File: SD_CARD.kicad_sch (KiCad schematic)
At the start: 6 parts, among them IC1 ECP5-BGA256, J4 Micro_SD_Card, U7 OSC_25M

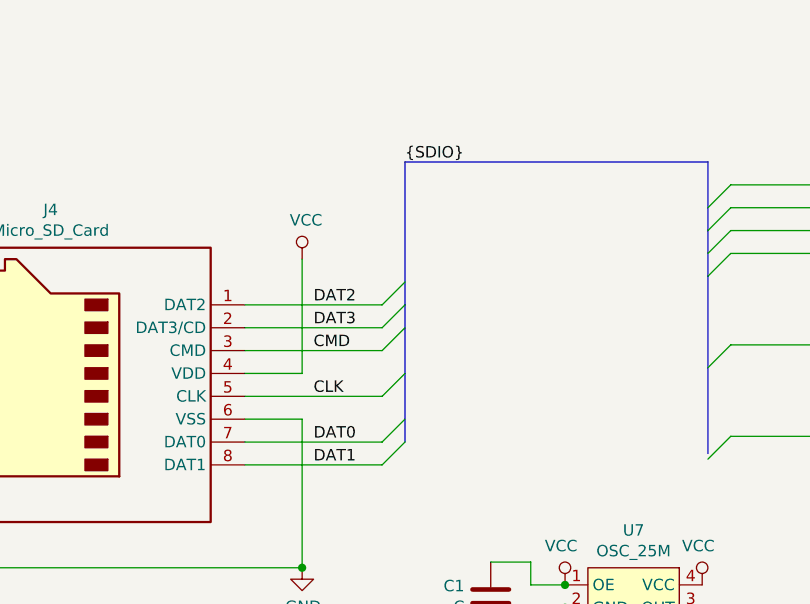
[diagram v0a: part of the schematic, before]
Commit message: Add semi-critical resistor values
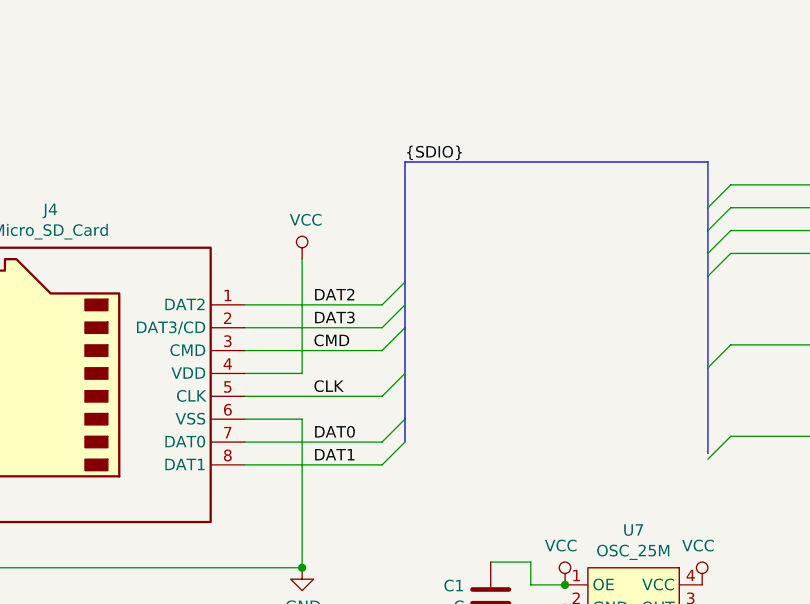
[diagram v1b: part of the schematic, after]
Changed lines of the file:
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@@
-(kicad_sch (version 20200618) (host eeschema "5.99.0-unknown-7340c97~102~ubuntu20.04.1")
-  (page 6 6)
+(kicad_sch (version 20200618) (host eeschema "5.99.0-unknown-e9da02e~102~ubuntu20.04.1")
+  (page 1 6)
   (paper "A4")
   (bus_alias "SDIO" (members "DAT[0..3]" "CMD" "CLK"))
@@
     (stroke (width 0) (type solid) (color 0 0 0 0))
   )
-  (bus (pts (xy 149.86 64.135) (xy 149.86 80.01))
+  (bus (pts (xy 149.86 64.135) (xy 149.86 77.47))
     (stroke (width 0) (type solid) (color 0 0 0 0))
   )
-  (bus (pts (xy 149.86 80.01) (xy 149.86 87.63))
+  (bus (pts (xy 149.86 77.47) (xy 149.86 82.55))
     (stroke (width 0) (type solid) (color 0 0 0 0))
   )
-  (bus (pts (xy 149.86 87.63) (xy 149.86 95.25))
+  (bus (pts (xy 149.86 82.55) (xy 149.86 92.71))
     (stroke (width 0) (type solid) (color 0 0 0 0))
   )
+  (bus (pts (xy 149.86 92.71) (xy 149.86 95.25))
+    (stroke (width 0) (type solid) (color 0 0 0 0))
+  )

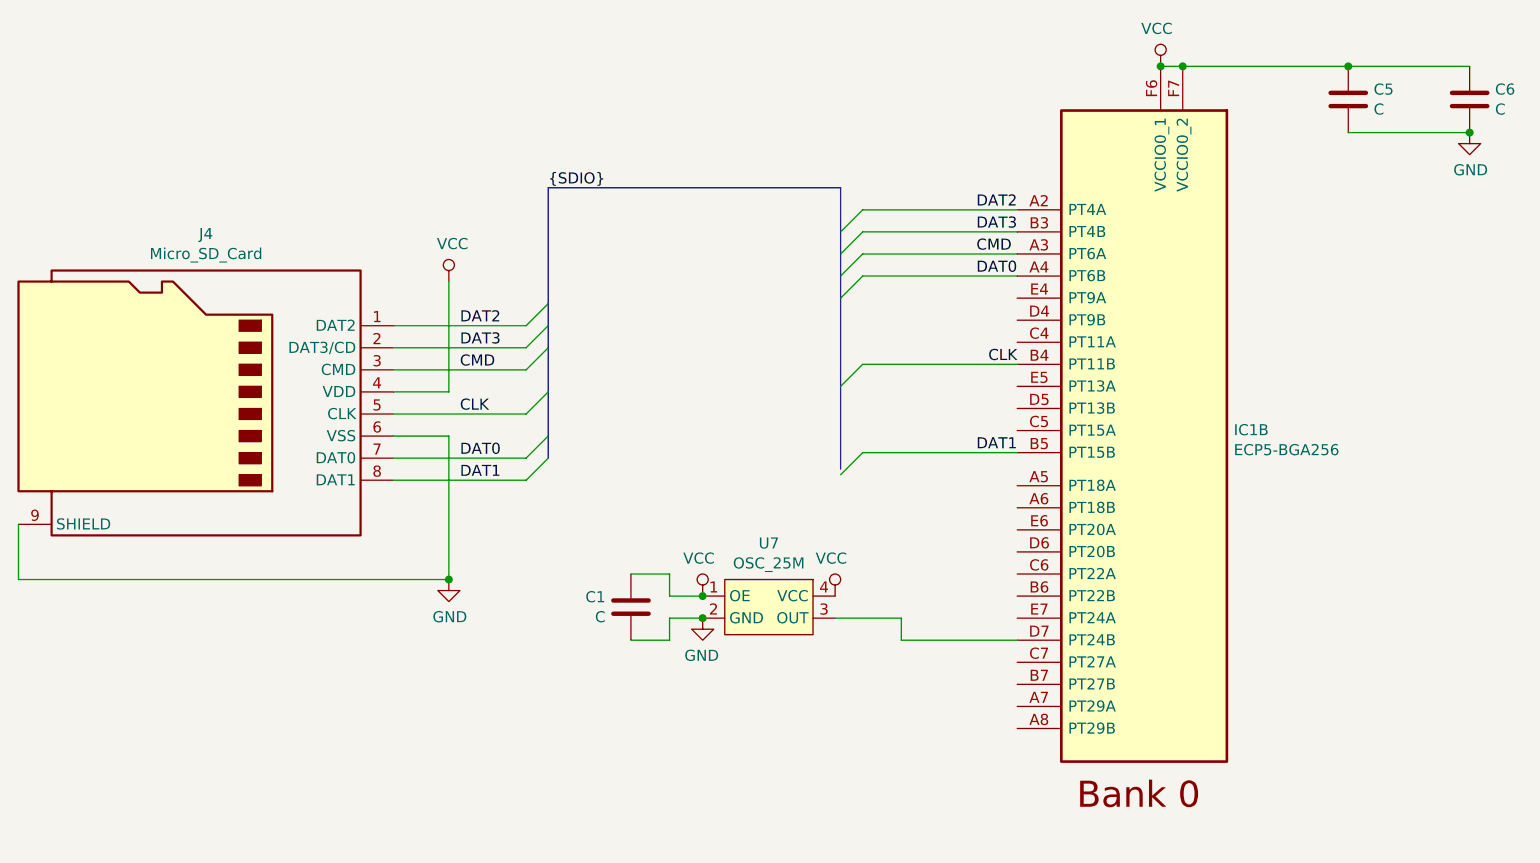
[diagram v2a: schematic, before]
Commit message: Change oscillator to SI5315, change RGB LED
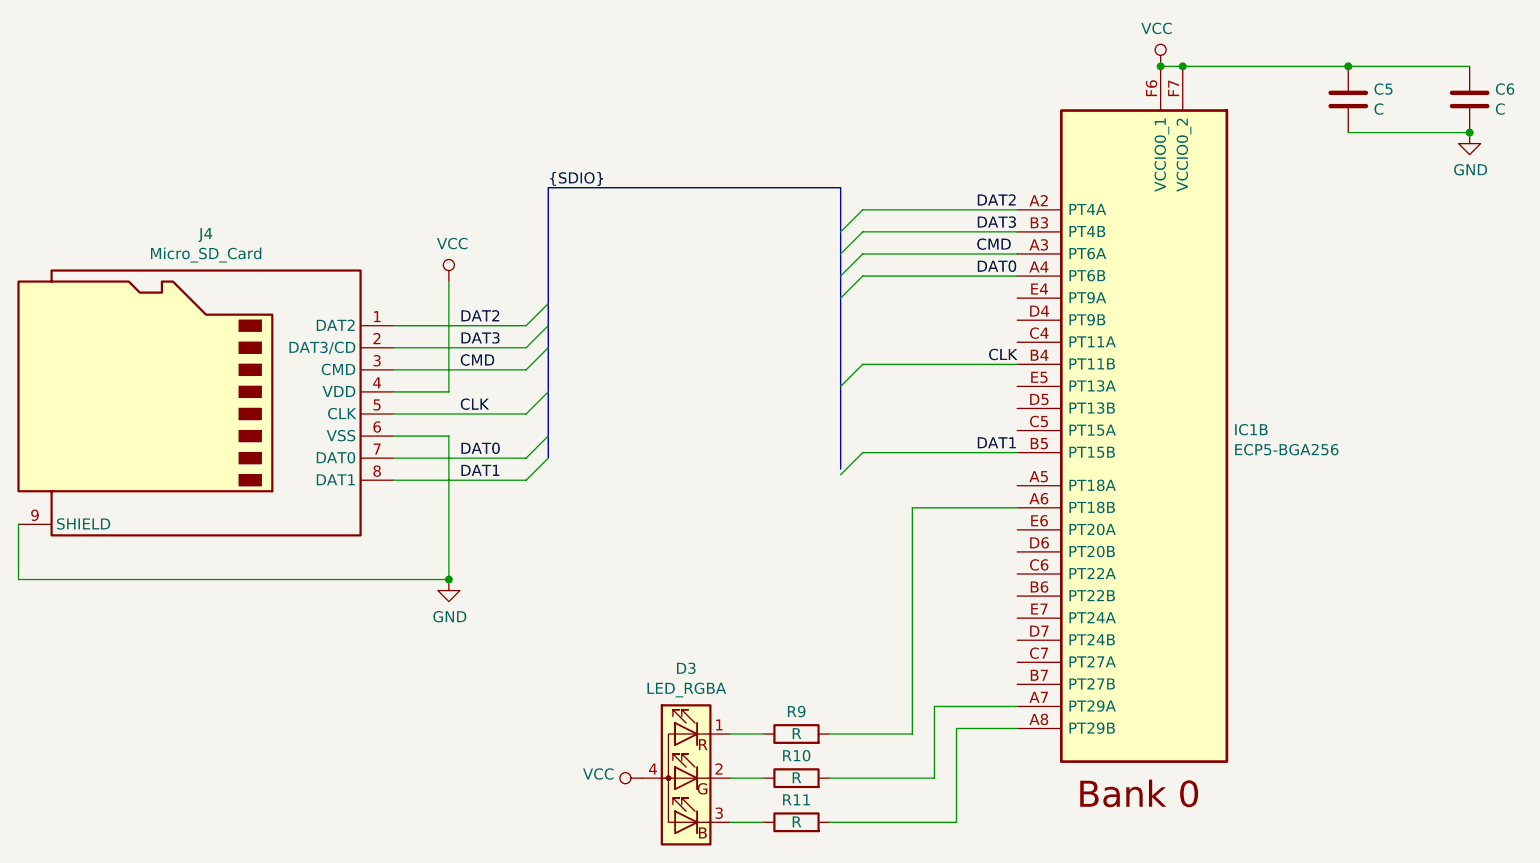
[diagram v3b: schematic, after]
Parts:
- removed C1: C, Capacitor_SMD:C_0402_1005Metric, symbol Device:C
- removed U7: OSC_25M, mini-mipi:SOIC-4, symbol mini_mipi:OSC_25M
- added D3: LED_RGBA, mini-mipi:LED_0404, symbol Device:LED_RGBA
- added R10, R11, R9: R, Resistor_SMD:R_0402_1005Metric, symbol Device:R
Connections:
- net VCC: now also D3.4 (A)
- net at IC1.A6 (PT18B): now also R9.2
- net at IC1.A7 (PT29A): now also R10.2
- net at IC1.A8 (PT29B): now also R11.2
- new net: D3.1 (RK), R9.1
- new net: D3.2 (GK), R10.1
- new net: D3.3 (BK), R11.1
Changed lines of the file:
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@@
-(kicad_sch (version 20200714) (host eeschema "5.99.0-unknown-9f20c61~102~ubuntu20.04.1")
-  (page 1 6)
+(kicad_sch (version 20200714) (host eeschema "5.99.0-unknown-20c1492~102~ubuntu20.04.1")
+  (page 6 6)
   (paper "A4")
   (bus_alias "SDIO" (members "DAT[0..3]" "CMD" "CLK"))
   (junction (at 138.43 109.22) (diameter 0) (color 0 0 0 0))
-  (junction (at 167.64 111.125) (diameter 0) (color 0 0 0 0))
-  (junction (at 167.64 113.665) (diameter 0) (color 0 0 0 0))
   (junction (at 220.345 50.165) (diameter 0) (color 0 0 0 0))
   (junction (at 222.885 50.165) (diameter 0) (color 0 0 0 0))
@@
     (stroke (width 0) (type solid) (color 0 0 0 0))
   )
-  (wire (pts (xy 159.385 116.205) (xy 163.83 116.205))
-    (stroke (width 0) (type solid) (color 0 0 0 0))
-  )
-  (wire (pts (xy 163.83 108.585) (xy 159.385 108.585))
-    (stroke (width 0) (type solid) (color 0 0 0 0))
-  )
-  (wire (pts (xy 163.83 111.125) (xy 163.83 108.585))
-    (stroke (width 0) (type solid) (color 0 0 0 0))
-  )
-  (wire (pts (xy 163.83 113.665) (xy 167.64 113.665))
-    (stroke (width 0) (type solid) (color 0 0 0 0))
-  )
-  (wire (pts (xy 163.83 116.205) (xy 163.83 113.665))
-    (stroke (width 0) (type solid) (color 0 0 0 0))
-  )
-  (wire (pts (xy 167.64 111.125) (xy 163.83 111.125))
+  (wire (pts (xy 170.815 127) (xy 174.625 127))
+    (stroke (width 0) (type solid) (color 0 0 0 0))
+  )
+  (wire (pts (xy 170.815 132.08) (xy 174.625 132.08))
+    (stroke (width 0) (type solid) (color 0 0 0 0))
+  )
+  (wire (pts (xy 170.815 137.16) (xy 174.625 137.16))
+    (stroke (width 0) (type solid) (color 0 0 0 0))
+  )
+  (wire (pts (xy 182.245 132.08) (xy 194.31 132.08))
     (stroke (width 0) (type solid) (color 0 0 0 0))
   )
@@
     (stroke (width 0) (type solid) (color 0 0 0 0))
   )
-  (wire (pts (xy 190.5 113.665) (xy 182.88 113.665))
-    (stroke (width 0) (type solid) (color 0 0 0 0))
-  )
-  (wire (pts (xy 190.5 116.205) (xy 190.5 113.665))
-    (stroke (width 0) (type solid) (color 0 0 0 0))
-  )
-  (wire (pts (xy 203.835 116.205) (xy 190.5 116.205))
+  (wire (pts (xy 191.77 100.965) (xy 191.77 127))
+    (stroke (width 0) (type solid) (color 0 0 0 0))
+  )
+  (wire (pts (xy 191.77 100.965) (xy 203.835 100.965))
+    (stroke (width 0) (type solid) (color 0 0 0 0))
+  )
+  (wire (pts (xy 191.77 127) (xy 182.245 127))
+    (stroke (width 0) (type solid) (color 0 0 0 0))
+  )
+  (wire (pts (xy 194.31 123.825) (xy 203.835 123.825))
+    (stroke (width 0) (type solid) (color 0 0 0 0))
+  )
+  (wire (pts (xy 194.31 132.08) (xy 194.31 123.825))
+    (stroke (width 0) (type solid) (color 0 0 0 0))
+  )
+  (wire (pts (xy 196.85 126.365) (xy 196.85 137.16))
+    (stroke (width 0) (type solid) (color 0 0 0 0))
+  )
+  (wire (pts (xy 196.85 137.16) (xy 182.245 137.16))
+    (stroke (width 0) (type solid) (color 0 0 0 0))
+  )
+  (wire (pts (xy 203.835 126.365) (xy 196.85 126.365))
     (stroke (width 0) (type solid) (color 0 0 0 0))
   )
@@
     (stroke (width 0) (type solid) (color 0 0 0 0))
   )
-  (bus (pts (xy 149.86 64.135) (xy 149.86 77.47))
-    (stroke (width 0) (type solid) (color 0 0 0 0))
-  )
-  (bus (pts (xy 149.86 77.47) (xy 149.86 82.55))
+  (bus (pts (xy 149.86 64.135) (xy 149.86 80.01))
+    (stroke (width 0) (type solid) (color 0 0 0 0))
+  )
+  (bus (pts (xy 149.86 80.01) (xy 149.86 82.55))
     (stroke (width 0) (type solid) (color 0 0 0 0))
   )
@@
     (stroke (width 0) (type solid) (color 0 0 0 0))
   )
-  (bus (pts (xy 183.515 64.135) (xy 183.515 71.755))
-    (stroke (width 0) (type solid) (color 0 0 0 0))
-  )
-  (bus (pts (xy 183.515 71.755) (xy 183.515 76.835))
-    (stroke (width 0) (type solid) (color 0 0 0 0))
-  )
-  (bus (pts (xy 183.515 76.835) (xy 183.515 96.52))
+  (bus (pts (xy 183.515 64.135) (xy 183.515 69.215))
+    (stroke (width 0) (type solid) (color 0 0 0 0))
+  )
+  (bus (pts (xy 183.515 69.215) (xy 183.515 74.295))
+    (stroke (width 0) (type solid) (color 0 0 0 0))
+  )
+  (bus (pts (xy 183.515 74.295) (xy 183.515 86.995))
+    (stroke (width 0) (type solid) (color 0 0 0 0))
+  )
+  (bus (pts (xy 183.515 86.995) (xy 183.515 96.52))
     (stroke (width 0) (type solid) (color 0 0 0 0))
   )
@@
     )
   )
-  (symbol (lib_id "power:VCC") (at 167.64 111.125 0) (mirror y) (unit 1)
-    (in_bom yes) (on_board yes)
-    (property "Reference" "#PWR0110" (id 0) (at 167.64 114.935 0)
-      (effects (font (size 1.27 1.27)) hide)
-    )
-    (property "Value" "VCC" (id 1) (at 167.2082 106.8006 0))
-    (property "Footprint" "" (id 2) (at 167.64 111.125 0)
-      (effects (font (size 1.27 1.27)) hide)
-    )
-    (property "Datasheet" "" (id 3) (at 167.64 111.125 0)
-      (effects (font (size 1.27 1.27)) hide)
-    )
-  )
-  (symbol (lib_id "power:VCC") (at 182.88 111.125 0) (mirror y) (unit 1)
-    (in_bom yes) (on_board yes)
-    (property "Reference" "#PWR0120" (id 0) (at 182.88 114.935 0)
-      (effects (font (size 1.27 1.27)) hide)
-    )
-    (property "Value" "VCC" (id 1) (at 182.4482 106.8006 0))
-    (property "Footprint" "" (id 2) (at 182.88 111.125 0)
-      (effects (font (size 1.27 1.27)) hide)
-    )
-    (property "Datasheet" "" (id 3) (at 182.88 111.125 0)
+  (symbol (lib_id "power:VCC") (at 160.655 132.08 90) (unit 1)
+    (in_bom yes) (on_board yes)
+    (property "Reference" "#PWR0150" (id 0) (at 164.465 132.08 0)
+      (effects (font (size 1.27 1.27)) hide)
+    )
+    (property "Value" "VCC" (id 1) (at 157.4799 131.6482 90)
+      (effects (font (size 1.27 1.27)) (justify left))
+    )
+    (property "Footprint" "" (id 2) (at 160.655 132.08 0)
+      (effects (font (size 1.27 1.27)) hide)
+    )
+    (property "Datasheet" "" (id 3) (at 160.655 132.08 0)
       (effects (font (size 1.27 1.27)) hide)
     )
@@
     )
   )
-  (symbol (lib_id "power:GND") (at 167.64 113.665 0) (mirror y) (unit 1)
-    (in_bom yes) (on_board yes)
-    (property "Reference" "#PWR0119" (id 0) (at 167.64 120.015 0)
-      (effects (font (size 1.27 1.27)) hide)
-    )
-    (property "Value" "GND" (id 1) (at 167.5257 117.9894 0))
-    (property "Footprint" "" (id 2) (at 167.64 113.665 0)
-      (effects (font (size 1.27 1.27)) hide)
-    )
-    (property "Datasheet" "" (id 3) (at 167.64 113.665 0)
-      (effects (font (size 1.27 1.27)) hide)
-    )
-  )
   (symbol (lib_id "power:GND") (at 255.905 57.785 0) (unit 1)
     (in_bom yes) (on_board yes)
@@
     )
   )
-  (symbol (lib_id "Device:C") (at 159.385 112.395 0) (mirror y) (unit 1)
-    (in_bom yes) (on_board yes)
-    (property "Reference" "C1" (id 0) (at 156.4639 111.2456 0)
-      (effects (font (size 1.27 1.27)) (justify left))
-    )
-    (property "Value" "C" (id 1) (at 156.4639 113.5443 0)
-      (effects (font (size 1.27 1.27)) (justify left))
-    )
-    (property "Footprint" "Capacitor_SMD:C_0402_1005Metric" (id 2) (at 158.4198 116.205 0)
-      (effects (font (size 1.27 1.27)) hide)
-    )
-    (property "Datasheet" "~" (id 3) (at 159.385 112.395 0)
+  (symbol (lib_id "Device:R") (at 178.435 127 90) (unit 1)
+    (in_bom yes) (on_board yes)
+    (property "Reference" "R9" (id 0) (at 178.435 124.46 90))
+    (property "Value" "R" (id 1) (at 178.435 127 90))
+    (property "Footprint" "Resistor_SMD:R_0402_1005Metric" (id 2) (at 178.435 128.778 90)
+      (effects (font (size 1.27 1.27)) hide)
+    )
+    (property "Datasheet" "~" (id 3) (at 178.435 127 0)
+      (effects (font (size 1.27 1.27)) hide)
+    )
+  )
+  (symbol (lib_id "Device:R") (at 178.435 132.08 90) (unit 1)
+    (in_bom yes) (on_board yes)
+    (property "Reference" "R10" (id 0) (at 178.435 129.54 90))
+    (property "Value" "R" (id 1) (at 178.435 132.08 90))
+    (property "Footprint" "Resistor_SMD:R_0402_1005Metric" (id 2) (at 178.435 133.858 90)
+      (effects (font (size 1.27 1.27)) hide)
+    )
+    (property "Datasheet" "~" (id 3) (at 178.435 132.08 0)
+      (effects (font (size 1.27 1.27)) hide)
+    )
+  )
+  (symbol (lib_id "Device:R") (at 178.435 137.16 90) (unit 1)
+    (in_bom yes) (on_board yes)
+    (property "Reference" "R11" (id 0) (at 178.435 134.62 90))
+    (property "Value" "R" (id 1) (at 178.435 137.16 90))
+    (property "Footprint" "Resistor_SMD:R_0402_1005Metric" (id 2) (at 178.435 138.938 90)
+      (effects (font (size 1.27 1.27)) hide)
+    )
+    (property "Datasheet" "~" (id 3) (at 178.435 137.16 0)
       (effects (font (size 1.27 1.27)) hide)
     )
@@
     )
   )
-  (symbol (lib_id "mini_mipi:OSC_25M") (at 175.26 109.22 0) (unit 1)
-    (in_bom yes) (on_board yes)
-    (property "Reference" "U7" (id 0) (at 175.26 105.0608 0))
-    (property "Value" "OSC_25M" (id 1) (at 175.26 107.3595 0))
-    (property "Footprint" "mini-mipi:SOIC-4" (id 2) (at 174.625 101.6 0)
-      (effects (font (size 1.27 1.27)) hide)
-    )
-    (property "Datasheet" "" (id 3) (at 174.625 101.6 0)
-      (effects (font (size 1.27 1.27)) hide)
-    )
+  (symbol (lib_id "Device:LED_RGBA") (at 165.735 132.08 0) (mirror y) (unit 1)
+    (in_bom yes) (on_board yes)
+    (property "Reference" "D3" (id 0) (at 165.735 119.4878 0))
+    (property "Value" "LED_RGBA" (id 1) (at 165.735 121.7865 0))
+    (property "Footprint" "mini-mipi:LED_0404" (id 2) (at 165.735 133.35 0)
+      (effects (font (size 1.27 1.27)) hide)
+    )
+    (property "Datasheet" "~" (id 3) (at 165.735 133.35 0)
+      (effects (font (size 1.27 1.27)) hide)
+    )
